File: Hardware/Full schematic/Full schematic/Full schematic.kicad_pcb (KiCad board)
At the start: 2 copper layers, 329 parts, among them J1 Conn_01x02_Male, J10 Conn_01x01_Male, J2 Reset, J3 Encoder, J4 Failure LED, J5 Bluetooth, J6 Conn_01x02_Male, J7 Display, J8 Buttons, J9 Conn_01x02_Male, K1 EDR101A0500, K2 EDR101A0500, K3 EDR101A0500, K4 EDR101A0500, K5 EDR101A0500, K6 EDR101A0500, Q1 BC847, Q10 IRLML6402, Q11 BC847, Q12 IRFZ44, Q13 BC847, Q14 BSS138, Q15 BC847, Q16 IRF610, Q17 BC847, Q18 IRLML6402, Q19 BC847, Q2 BC847, Q20 BFS17, Q21 IRLML6402, Q22 AFT05MS003N, Q23 IRLML2502, Q24 IRLML2502, Q25 IRLML2502, Q26 IRLML2502, Q27 IRLML2502, Q28 IRLML2502, Q3 BC847, Q4 BC847, Q5 BC847, Q6 IRLML6402, Q7 IRF4905, Q8 IRLML6402, Q9 IRLML6402, U1 74LVC2T45DC, U10 ICS501, U11 STM32F103C8Tx, U12 CAT24C256, U2 74LVC2T45DC, U3 AD9835, U4 LM27313XMF, U5 LM2734X, U6 LM2734X, U7 LM2734X, U8 UC3843_SOIC8, U9 AD5245BRJZ10, X1 50MHz, Y1 8MHz, Y2 32768Hz

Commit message: PCB tracing in progress
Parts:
- moved C101 48.7 mm to (191.2, 167.6)
- moved C103 48.7 mm to (163.7, 129.7)
- moved C106 48.7 mm to (163.7, 135.8)
- moved C118 48.7 mm to (169.5, 135.8)
- moved C121 48.7 mm to (175.4, 129.7)
- moved C124 48.7 mm to (175.4, 135.8)
- moved C127 48.7 mm to (181.3, 129.7)
- moved C133 48.7 mm to (187.0, 129.7)
- moved C136 48.7 mm to (187.1, 135.8)
- moved C18 48.7 mm to (141.7, 165.2)
- moved C4 48.7 mm to (150.8, 170.6)
- moved C44 48.7 mm to (142.1, 151.7)
- moved C5 48.7 mm to (150.7, 164.4)
- moved C61 48.7 mm to (165.2, 164.1)
- moved C65 48.7 mm to (167.3, 164.0)
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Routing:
- net PWR_3.5_5: track 45.0 -> 222.5 mm, vias 0 -> 3
- net ACTIVATE_144: track 170.2 -> 315.5 mm
- net Manipulation: track 3.72 -> 137.6 mm, vias 2 -> 4
- net ADC_UANT: track 7.85 -> 141.6 mm, vias 1 -> 2
- net PWR_3.5_12: track 77.5 -> 200.5 mm, vias 6 -> 8
- net BATT_7.4V: track 101.5 -> 194.4 mm
- net DDS_FSYNC: track 2.38 -> 82.0 mm, vias 1 -> 2
- net PWR_3.5_OUT: track 17.6 -> 96.5 mm, vias 0 -> 2
- net REG_5V: track 170.2 -> 233.8 mm, vias 8 -> 11
- net DDS_SDATA: track 12.6 -> 61.3 mm, vias 2 -> 3
- net DDS_SCLK: track 9.50 -> 52.5 mm, vias 2 -> 3
- net GND: track 877.1 -> 913.6 mm, vias 28 -> 30
- net REG_3.3V: track 204.2 -> 228.3 mm
- net ENABLE_BT: track 44.3 -> 47.3 mm
- net BOOT1: track 11.3 -> 13.4 mm

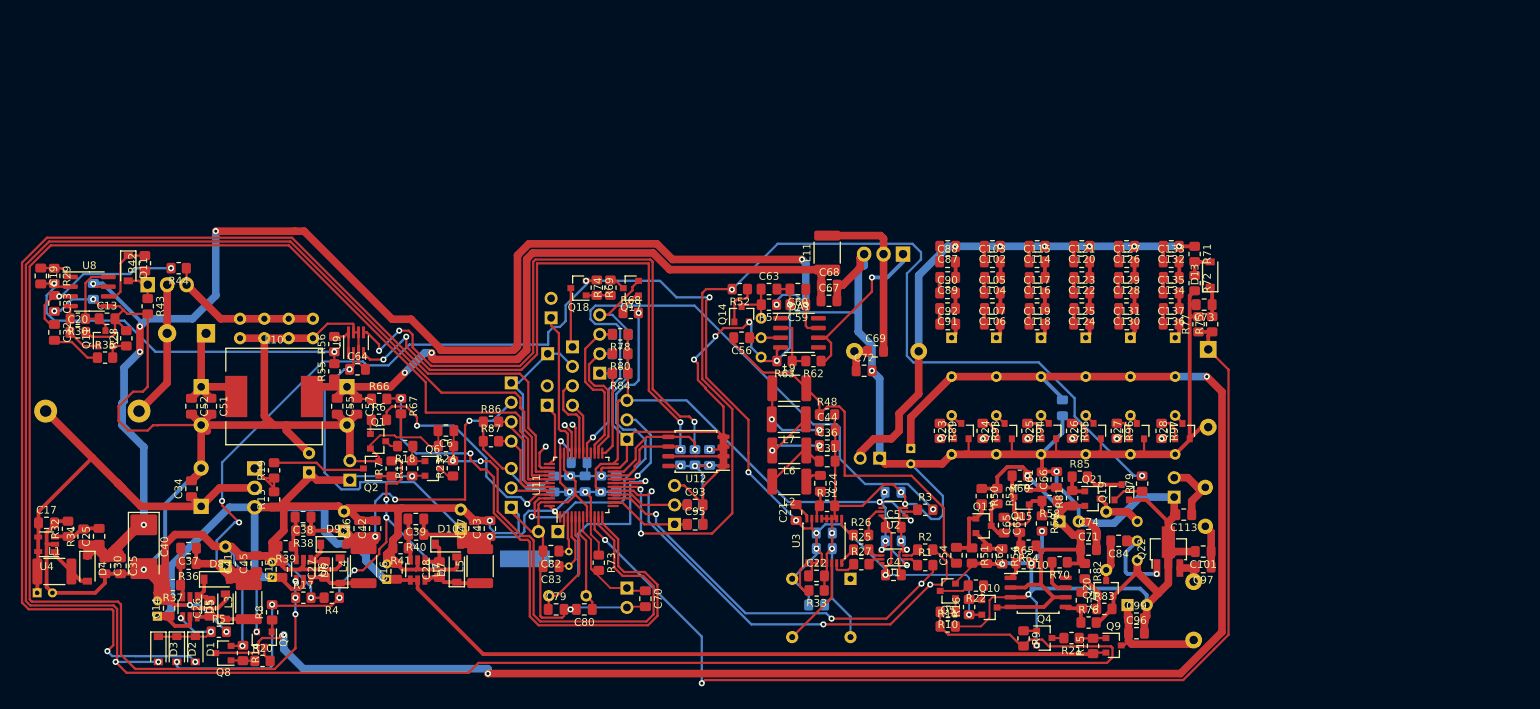
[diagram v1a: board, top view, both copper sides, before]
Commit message: PCB tracing - all parts are connected as needed
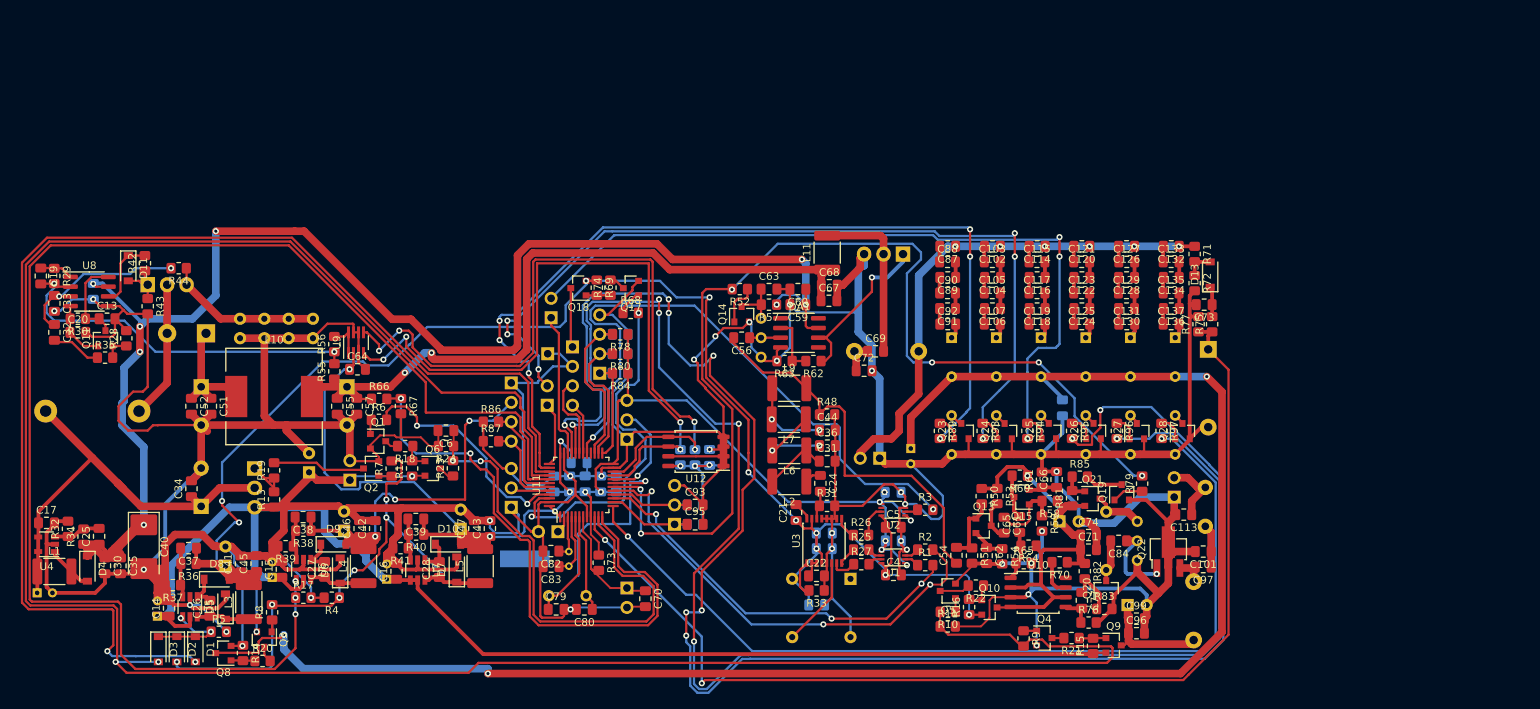
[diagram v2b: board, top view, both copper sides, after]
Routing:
- net MATCH_2: track 4.02 -> 224.0 mm, vias 2 -> 9
- net MATCH_1: track 3.87 -> 202.1 mm, vias 2 -> 6
- net MATCH_0: track 0.00 -> 118.2 mm, vias 1 -> 2
- net MATCH_5: track 4.26 -> 119.0 mm, vias 2 -> 6
- net MATCH_4: track 0.00 -> 111.7 mm, vias 1 -> 6
- net MATCH_3: track 0.00 -> 99.7 mm, vias 1 -> 3
- net GND: track 913.6 -> 916.3 mm
- net REG_5V: track 233.8 -> 232.8 mm
- net Manipulation: vias 4 -> 6

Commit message: PCB seems to be ready
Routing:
- net ACTIVATE_3.5: track 89.9 -> 107.5 mm
- net PWR_3.5_12: track 200.5 -> 188.5 mm
- net ACTIVATE_144: track 315.5 -> 324.4 mm
- net MATCH_2: track 224.0 -> 218.8 mm, vias 9 -> 7
- net MATCH_1: track 202.1 -> 196.9 mm
- net BATT_7.4V: track 194.4 -> 198.4 mm
- net PWR_3.5_5: track 222.5 -> 224.5 mm
- net MATCH_0: track 118.2 -> 119.7 mm
- net ADC_UANT: track 141.6 -> 142.9 mm
- net ACTIVATE_FOX: track 163.6 -> 164.8 mm
- net ACTIVATE_DISPLAY: track 183.8 -> 184.9 mm
- net GND: vias 30 -> 80
- added copper zone on B.Cu, net GND
- added copper zone on F.Cu, net GND
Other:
- board outline added: 159.3 x 59.9 mm
- board text added: "https://github.com/WhiteFossa/yiff-l"
